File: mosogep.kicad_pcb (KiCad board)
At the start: 2 copper layers, 100 x 100 mm, 262 parts, among them J1 Programozó csati, J2 AC1010, J3 RJ45_Amphenol_RJMG1BD3B8K1ANR, J4 AC1010, J5 AC1010, J6 AC1010, J7 line_in, Q1 yjl2301c, Q2 BC817, SW1 SW_DIP_x01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

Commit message: 3v3 finished
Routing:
- net +3.3VA: track 189.0 -> 207.0 mm, vias 17 -> 19
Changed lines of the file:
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@@
     (thickness 1.6)
     (drawings 20)
-    (tracks 1700)
+    (tracks 1710)
     (zones 0)
     (modules 262)
@@
   )
   (setup
-    (last_trace_width 0.25)
+    (last_trace_width 0.508)
     (user_trace_width 0.254)
     (user_trace_width 0.381)
@@
   (segment (start 80.485999 151.745999) (end 80.6 151.86) (width 0.508) (layer B.Cu) (net 9))
   (segment (start 76.954001 151.745999) (end 80.485999 151.745999) (width 0.508) (layer B.Cu) (net 9))
-  (segment (start 73.175 155.525) (end 76.954001 151.745999) (width 0.508) (layer B.Cu) (net 9))
+  (segment (start 62 150.058568) (end 63.091432 151.15) (width 0.508) (layer B.Cu) (net 9))
+  (segment (start 62 146.1) (end 62 150.058568) (width 0.508) (layer B.Cu) (net 9))
+  (segment (start 63.091432 151.15) (end 67 151.15) (width 0.508) (layer B.Cu) (net 9))
+  (segment (start 67 151.15) (end 68.25 152.4) (width 0.508) (layer B.Cu) (net 9))
+  (via (at 70.9 152.4) (size 0.8) (drill 0.4) (layers F.Cu B.Cu) (net 9))
+  (segment (start 68.25 152.4) (end 70.9 152.4) (width 0.508) (layer B.Cu) (net 9))
+  (segment (start 72.275 152.4) (end 74.2875 154.4125) (width 0.508) (layer F.Cu) (net 9))
+  (via (at 74.2875 154.4125) (size 0.8) (drill 0.4) (layers F.Cu B.Cu) (net 9))
+  (segment (start 74.2875 154.4125) (end 76.954001 151.745999) (width 0.508) (layer B.Cu) (net 9))
+  (segment (start 70.9 152.4) (end 72.275 152.4) (width 0.508) (layer F.Cu) (net 9))
+  (segment (start 73.175 155.525) (end 74.2875 154.4125) (width 0.508) (layer B.Cu) (net 9))
   (segment (start 50.716 176.642) (end 50.716 175.577) (width 0.508) (layer B.Cu) (net 10))
   (segment (start 50.716 178.152) (end 50.716 176.642) (width 0.508) (layer B.Cu) (net 10))

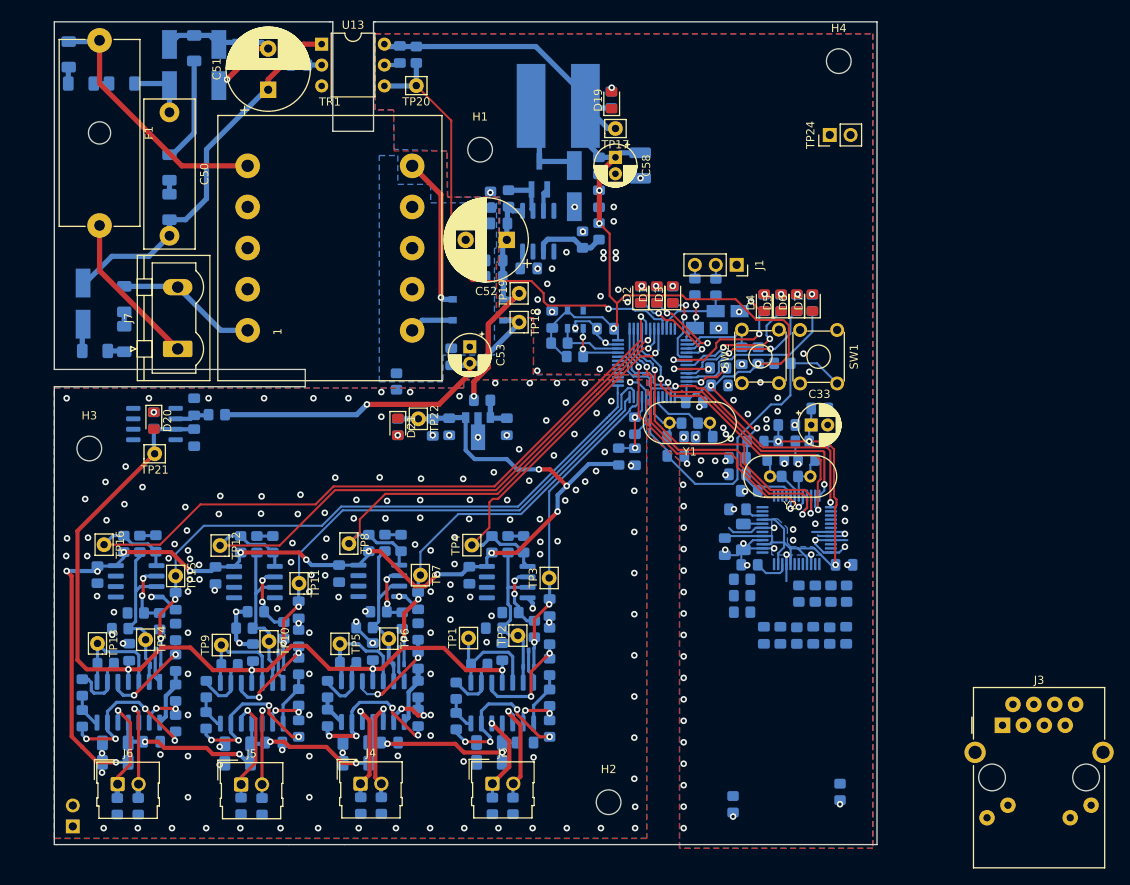
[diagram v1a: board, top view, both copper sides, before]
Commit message: front silk
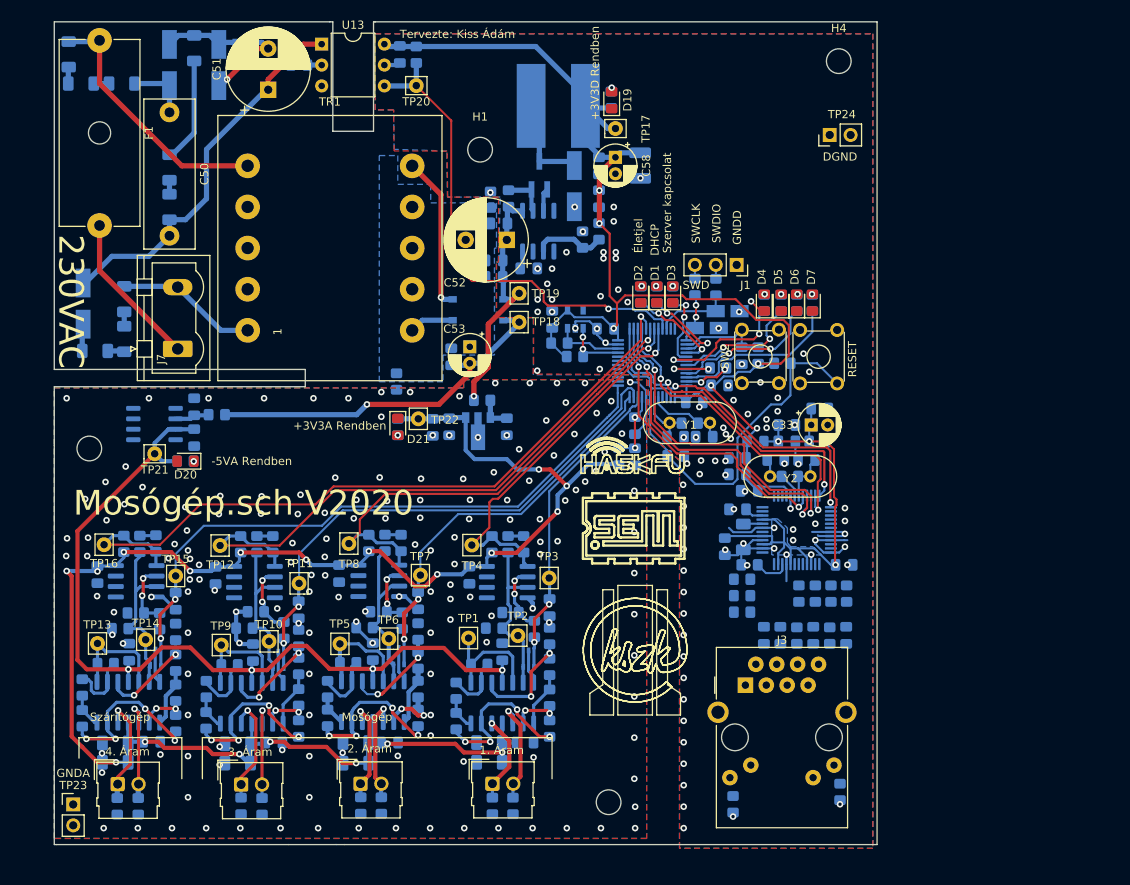
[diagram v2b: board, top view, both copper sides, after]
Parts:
- TP23: moved to F.Cu
- moved J3 31.6 mm to (96.0, 178.6)
- moved R103 6.26 mm to (27.9, 151.4), turned to 180 degrees
- moved D20 6.25 mm to (27.9, 151.4), turned to 180 degrees
- moved TP23 2.67 mm to (14.3, 193.1)
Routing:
- net -3V3: track 106.5 -> 108.4 mm
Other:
- board text added: "GNDD"
- board text added: "Mosógép"
- board text added: "Mosógép.sch V2020"
- board text added: "SWCLK"
- board text added: "SWDIO"
- board text added: "Szárítógép"
- board text added: "Tervezte: Kiss Ádám"

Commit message: Bottom silk
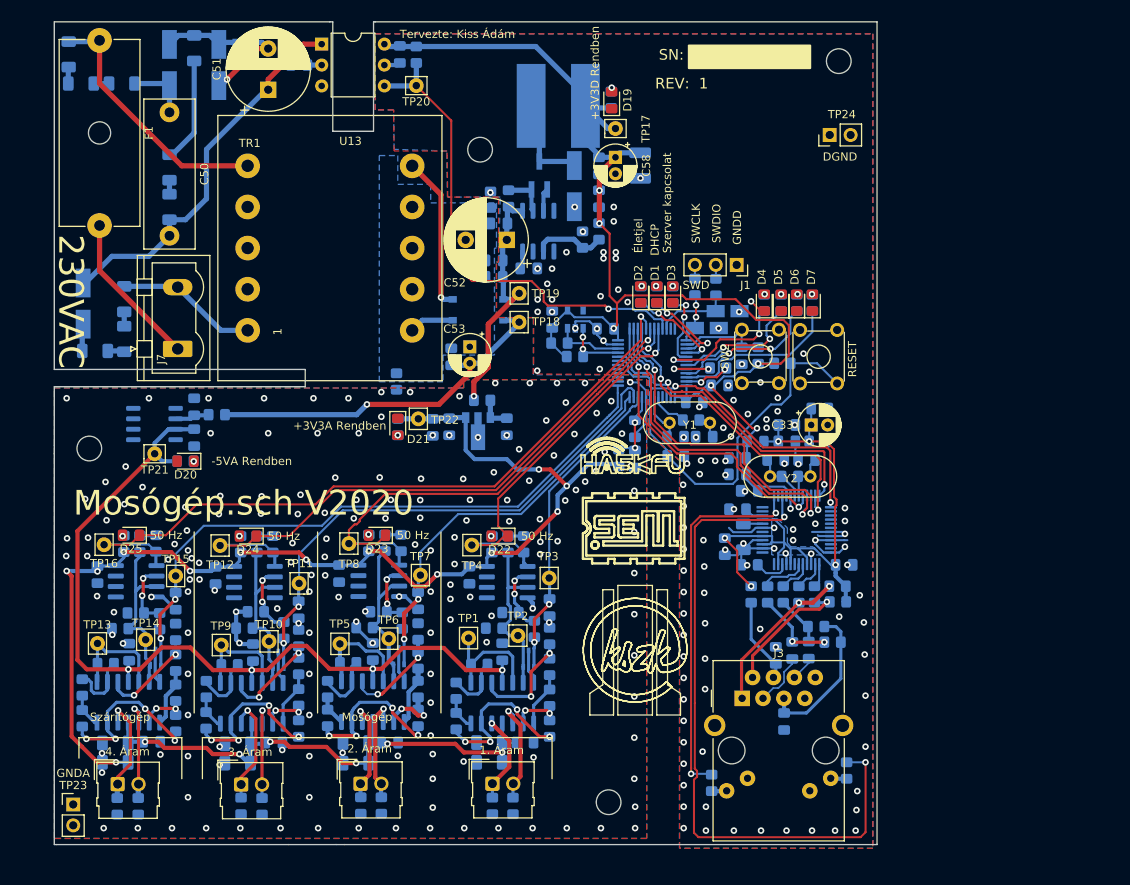
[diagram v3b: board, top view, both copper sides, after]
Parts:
- added D22: LED, LED_SMD:LED_0805_2012Metric_Pad1.15x1.40mm_HandSolder, F.Cu at (66.1, 160.5)
- added D23: LED, LED_SMD:LED_0805_2012Metric_Pad1.15x1.40mm_HandSolder, F.Cu at (51.2, 160.4)
- added D24: LED, LED_SMD:LED_0805_2012Metric_Pad1.15x1.40mm_HandSolder, F.Cu at (35.5, 160.5)
- added D25: LED, LED_SMD:LED_0805_2012Metric_Pad1.15x1.40mm_HandSolder, F.Cu at (21.3, 160.4)
- C61: value C -> 100n
- F1: value Fuse -> 100mA
- J3: value RJ45_Amphenol_RJMG1BD3B8K1ANR -> RB1-1D6B8K1A
- R106, R107, R108, R109, R110, R111, R90, R91, R92: value 22k/3 -> 7k2
- R11: value 1M -> 470
- moved C25 12.9 mm to (100.7, 183.0), turned to 270 degrees
- moved R37 11.7 mm to (107.2, 168.5), turned to 180 degrees
- moved R40 11.6 mm to (107.2, 166.6), turned to 180 degrees
- moved R41 4.42 mm to (106.6, 173.4), turned to 0 degrees
- moved C30 3.91 mm to (101.7, 174.4)
- moved R34 3.90 mm to (102.5, 167.6)
- moved R35 3.90 mm to (100.6, 167.6)
- moved R33 3.90 mm to (104.4, 167.6)
- moved R36 3.80 mm to (98.7, 167.6)
- moved R42 3.68 mm to (91.9, 190.5), turned to 90 degrees
- moved R43 2.72 mm to (108.3, 189.0), turned to 90 degrees
- moved C31 2.50 mm to (99.7, 175.0)
- moved R38 1.98 mm to (104.6, 171.5), turned to 0 degrees
- moved C28 1.88 mm to (103.7, 174.4)
- moved J3 1.65 mm to (95.6, 180.2)
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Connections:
- R11 pad 1: Net-(C5-Pad1) -> Net-(C2-Pad1)
- R11 pad 2: Net-(C2-Pad1) -> Net-(R11-Pad2)
- R30 pad 2: /fazisdetektor1 -> Net-(D22-Pad2)
- R59 pad 2: /fazisdetektor2 -> Net-(D23-Pad2)
- R74 pad 2: /fazisdetektor3 -> Net-(D24-Pad2)
- R89 pad 2: /fazisdetektor4 -> Net-(D25-Pad2)
- U2 pad 5: Net-(C2-Pad1) -> Net-(R11-Pad2)
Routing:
- net Net-(R43-Pad2): track 0.00 -> 83.6 mm, vias 1 -> 2
- net Net-(R42-Pad2): track 0.00 -> 45.9 mm, vias 1 -> 2
- net Net-(J3-PadR1): track 0.00 -> 19.1 mm, vias 0 -> 2
- net Net-(C25-Pad1): track 0.00 -> 18.4 mm
- net Net-(J3-PadR2): track 0.00 -> 15.9 mm, vias 0 -> 1
- net Net-(C21-Pad1): track 58.0 -> 70.3 mm, vias 3 -> 5
- net Net-(C31-Pad1): track 0.00 -> 10.5 mm
- net Net-(C30-Pad2): track 0.00 -> 9.95 mm, vias 0 -> 2
- net Net-(C30-Pad1): track 0.00 -> 6.62 mm
- net Net-(C2-Pad1): track 9.90 -> 3.34 mm
- net Net-(R36-Pad2): track 0.00 -> 6.22 mm
- net Net-(C28-Pad2): track 0.00 -> 6.07 mm
- net Net-(R35-Pad2): track 0.00 -> 4.72 mm
- net Net-(R11-Pad2): track 0.00 -> 4.60 mm
- net /fazisdetektor2: track 59.4 -> 63.5 mm
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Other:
- board text added: "JLC SN: JLCJLCJLCJLC"
- board text added: "REV: 1"
- board text added: "SN:"

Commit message: Krisztián megjegyzései 1
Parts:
- removed R111, R92: 7k2, Resistor_SMD:R_1206_3216Metric_Pad1.30x1.75mm_HandSolder
- C50: value 100n -> 560p; footprint Capacitor_THT:C_Rect_L18.0mm_W6.0mm_P15.00mm_FKS3_FKP3 -> Capacitor_SMD:C_1206_3216Metric_Pad1.33x1.80mm_HandSolder; moved to B.Cu
- C51: value 10u -> 330n; footprint Capacitor_THT:CP_Radial_D10.0mm_P5.00mm -> Capacitor_SMD:C_1206_3216Metric_Pad1.33x1.80mm_HandSolder; moved to B.Cu
- D14: value do-214AC -> bzd27c100; footprint Diode_SMD:D_SMA_Handsoldering -> Diode_SMD:D_MELF_Handsoldering
- D15: value do-214AC -> 5V6; footprint Diode_SMD:D_SMA_Handsoldering -> Diode_SMD:D_MiniMELF_Handsoldering
- D16: value do-214AC -> ll4148
- R106, R107, R108, R109, R90, R91: value 7k2 -> 82k
- R110: value 7k2 -> 470k
- R96: value 1k -> 220
- moved R100 28.6 mm to (60.1, 142.4), turned to 90 degrees
- moved D14 14.1 mm to (25.1, 122.0)
- moved C50 10.3 mm to (34.8, 103.6), turned to 90 degrees
- moved R110 8.10 mm to (25.1, 112.5), turned to 270 degrees
- moved R90 7.34 mm to (14.9, 130.9), turned to 270 degrees
- moved U14 5.96 mm to (21.8, 152.3)
- moved C62 5.96 mm to (26.6, 150.2)
- moved C64 5.96 mm to (26.6, 154.0)
- moved R103 5.96 mm to (25.5, 156.8)
- moved D20 5.96 mm to (25.6, 156.8)
- moved TP21 5.96 mm to (21.8, 155.9)
- moved R91 5.59 mm to (23.2, 100.8), turned to 270 degrees
- moved R107 4.16 mm to (16.4, 136.9), turned to 180 degrees
- moved Q2 4.11 mm to (39.1, 101.8)
- moved R106 3.69 mm to (21.2, 135.3)
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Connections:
- C51 pad 1: Net-(C50-Pad2) -> Net-(C50-Pad1)
- D15 pad 1: Net-(C50-Pad1) -> Net-(C51-Pad2)
- D15 pad 2: Net-(D15-Pad2) -> Net-(C50-Pad1)
- D16 pad 1: Net-(D15-Pad2) -> Net-(C50-Pad2)
- D16 pad 2: Net-(C51-Pad2) -> Net-(C50-Pad1)
- Q2 pad 1: Net-(D15-Pad2) -> Net-(C50-Pad2)
- Q2 pad 2: Net-(C51-Pad2) -> Net-(Q2-Pad2)
- Q2 pad 3: Net-(Q2-Pad3) -> Net-(C51-Pad2)
- R110 pad 1: Net-(C50-Pad2) -> Net-(C50-Pad1)
- R110 pad 2: Net-(R110-Pad2) -> Net-(C50-Pad2)
- R91 pad 1: Net-(C50-Pad1) -> Net-(C51-Pad2)
- R96 pad 2: Net-(Q2-Pad3) -> Net-(C50-Pad1)
- U13 pad 1: Net-(C50-Pad2) -> Net-(Q2-Pad2)
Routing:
- net Net-(C62-Pad2): track 4.21 -> 39.3 mm
- net Net-(C53-Pad2): track 45.6 -> 13.9 mm, vias 1 -> 0
- net Net-(C50-Pad2): track 46.4 -> 27.1 mm, vias 0 -> 2
- net Net-(C50-Pad1): track 7.60 -> 25.7 mm
- net Net-(R111-Pad1): track 12.8 -> 0.00 mm
- net Net-(C51-Pad2): track 10.2 -> 20.8 mm, vias 1 -> 2
- net Net-(D15-Pad2): track 9.06 -> 0.00 mm
- net Net-(D14-Pad2): track 3.29 -> 11.9 mm
- net Net-(Q2-Pad3): track 6.27 -> 0.00 mm
- net Net-(C52-Pad1): track 31.0 -> 25.4 mm, vias 1 -> 2
- net -3V3: track 108.4 -> 103.7 mm
- net Net-(Q2-Pad2): track 0.00 -> 4.47 mm
- net Net-(R109-Pad2): track 1.85 -> 5.66 mm
- net Net-(R108-Pad2): track 2.02 -> 4.61 mm
- net Net-(R107-Pad2): track 2.04 -> 4.44 mm
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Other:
- outline, holes or cut-outs redrawn

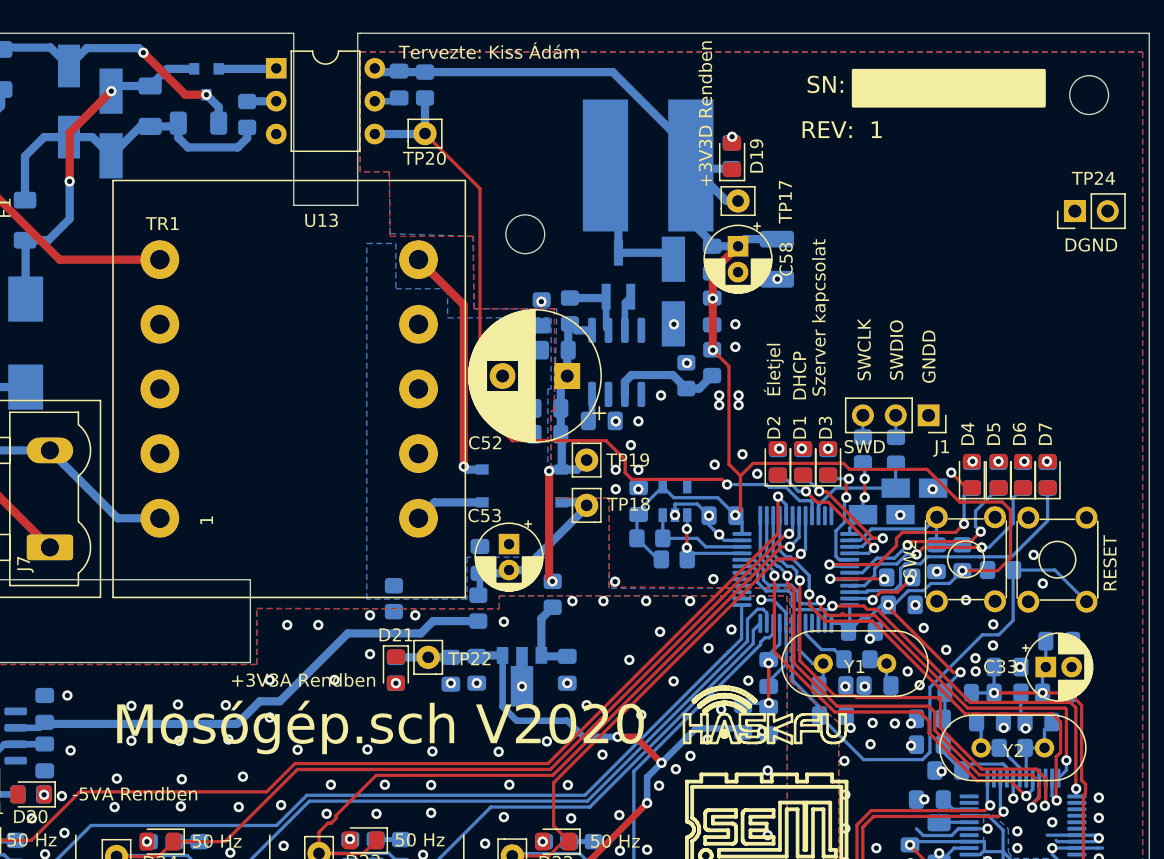
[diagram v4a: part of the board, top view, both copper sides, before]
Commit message: updated L2 value
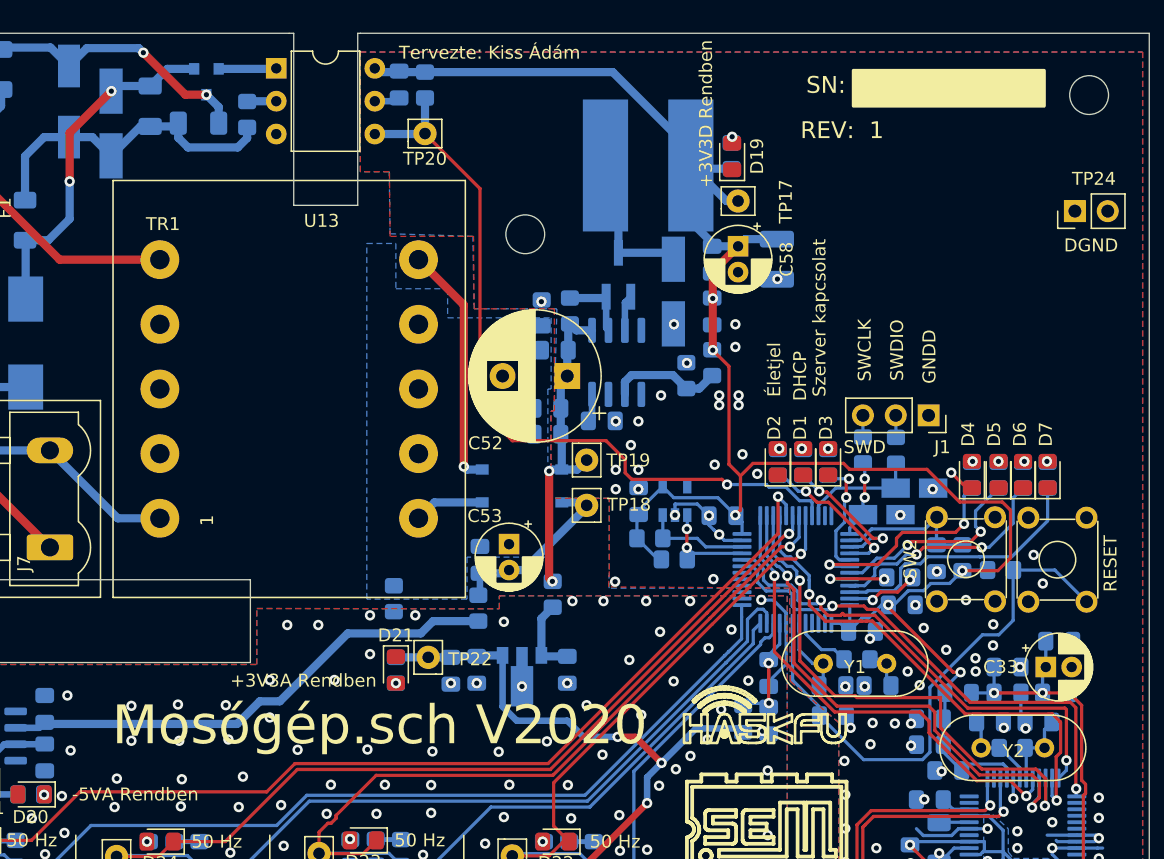
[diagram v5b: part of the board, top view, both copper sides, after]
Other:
- net class Default removed
